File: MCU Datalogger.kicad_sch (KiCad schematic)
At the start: 0 parts

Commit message: Setup of EESchema for new project
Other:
- title: (none) -> ${project_name}
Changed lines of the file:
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@@
 	(generator_version "9.0")
 	(paper "A4")
+	(title_block
+		(title "${project_name}")
+		(date "2025-10-13")
+		(rev "1.0")
+	)
 	(sheet_instances
 		(path "/"

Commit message: Required Symbols Added
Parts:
- added BT1: Battery, symbol Device:Battery
- added C1, C2, C3, C4: C, symbol Device:C
- added C5: C_Polarized, symbol Device:C_Polarized
- added D1, D2: LED, symbol Device:LED
- added H1, H2, H3, H4: MountingHole, symbol Mechanical:MountingHole
- added R1, R2, R3, R4, R5, R6, R7: R, symbol Device:R
- added U1, U2: 24LC1025, symbol Memory_EEPROM:24LC1025
- added U3: DS1337S_, DS1337S_:SOIC127P600X175-8N, symbol DS1337S_:DS1337S_
- added U4: ATMEGA328P-AU, ATMEGA328P-AU:QFP80P900X900X120-32N, symbol ATMEGA328P-AU:ATMEGA328P-AU
- added Y1, Y2: Crystal, symbol Device:Crystal
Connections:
- new net: U4.21 (GND), U4.3 (GND), U4.5 (GND)
- new net: U4.4 (VCC), U4.6 (VCC)
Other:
- added sheet Connectors (connectors.kicad_sch)

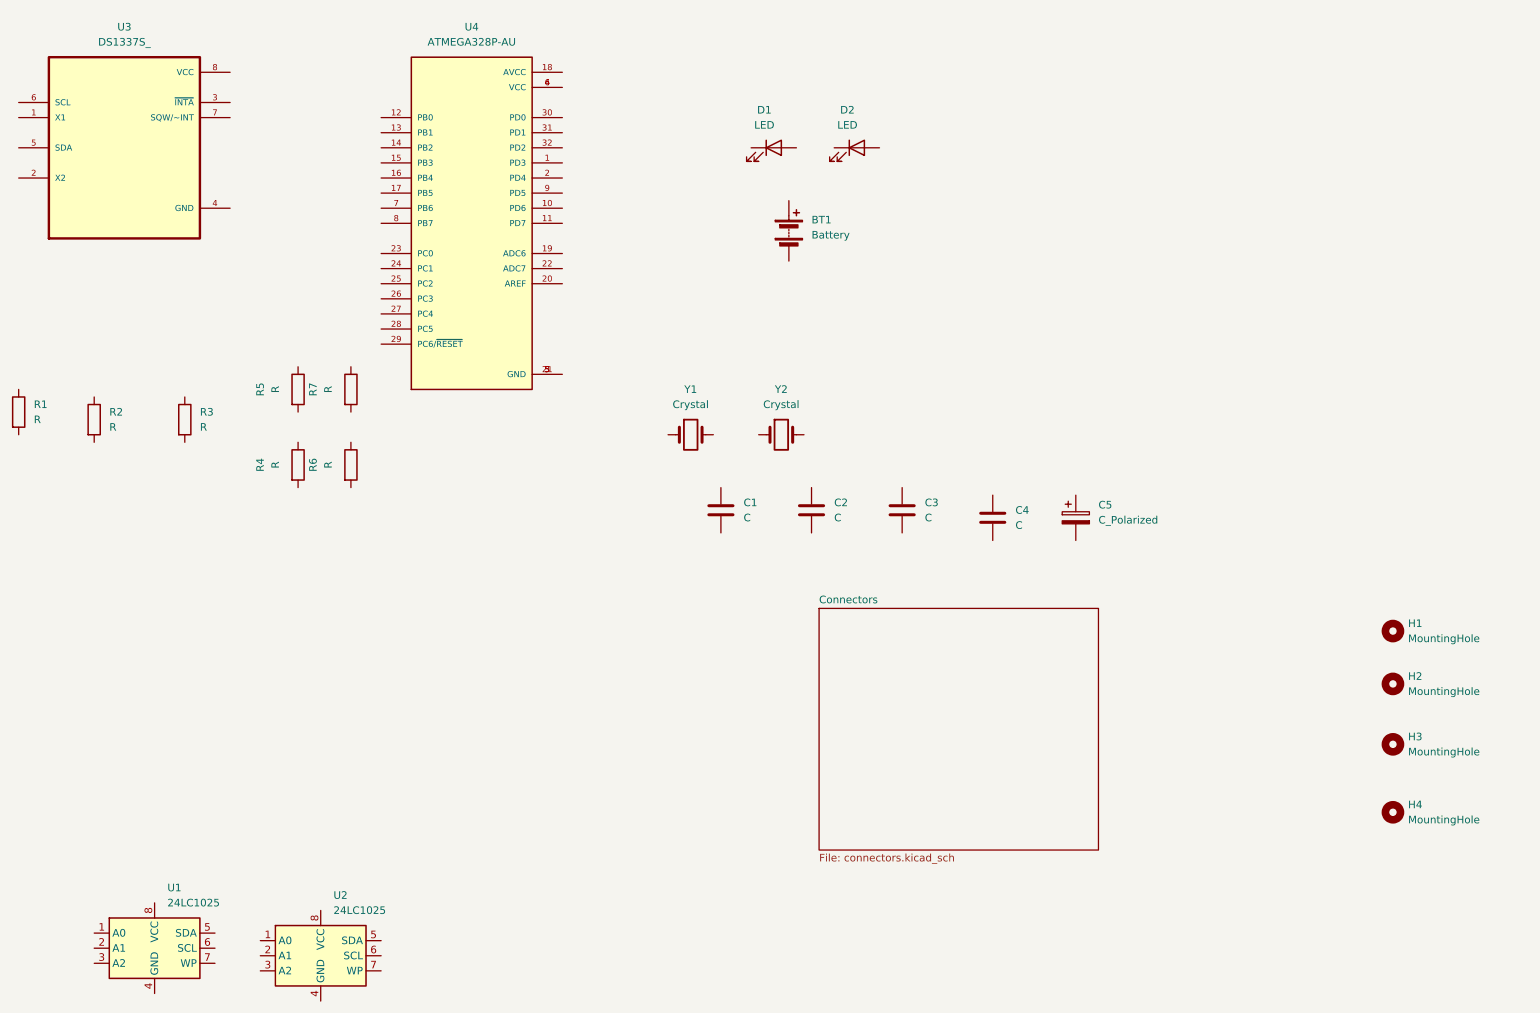
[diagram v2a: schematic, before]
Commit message: Change location of symbols
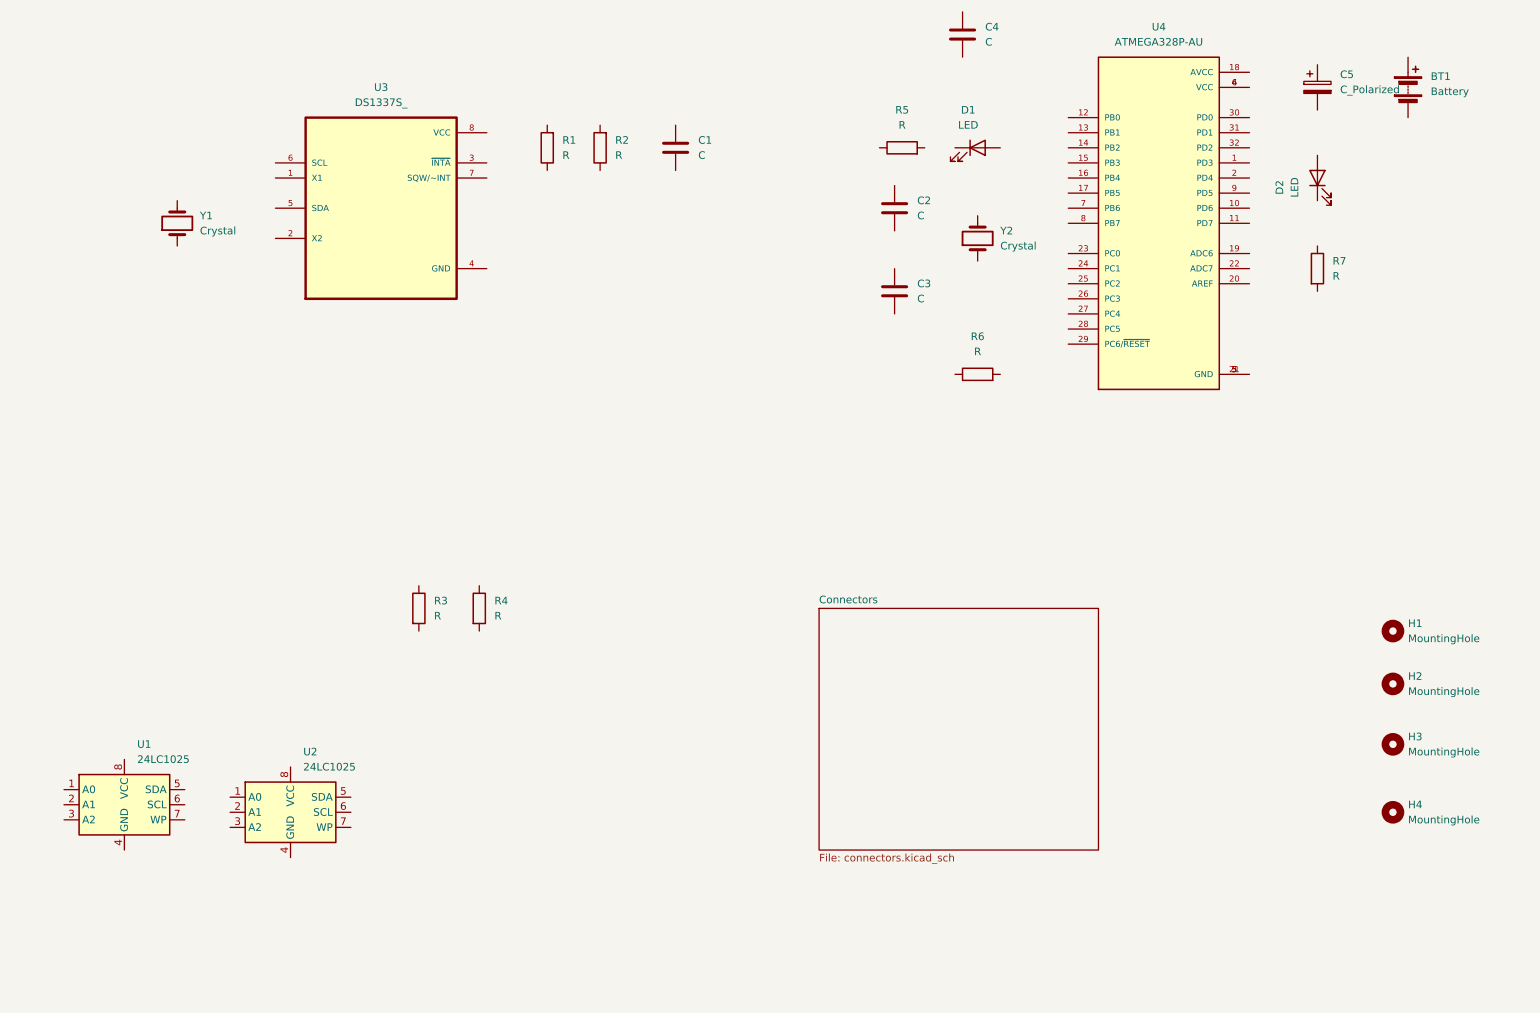
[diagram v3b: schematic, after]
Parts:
- renumbered D2 to D1, D1 to D2, R4 to R1, R6 to R2, R2 to R3, R3 to R4, R7 to R6, R1 to R7
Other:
- moved on the sheet: BT1, C1, C2, C3, C4, C5, D1, D2, R1, R2, R3, R4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

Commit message: Added components values
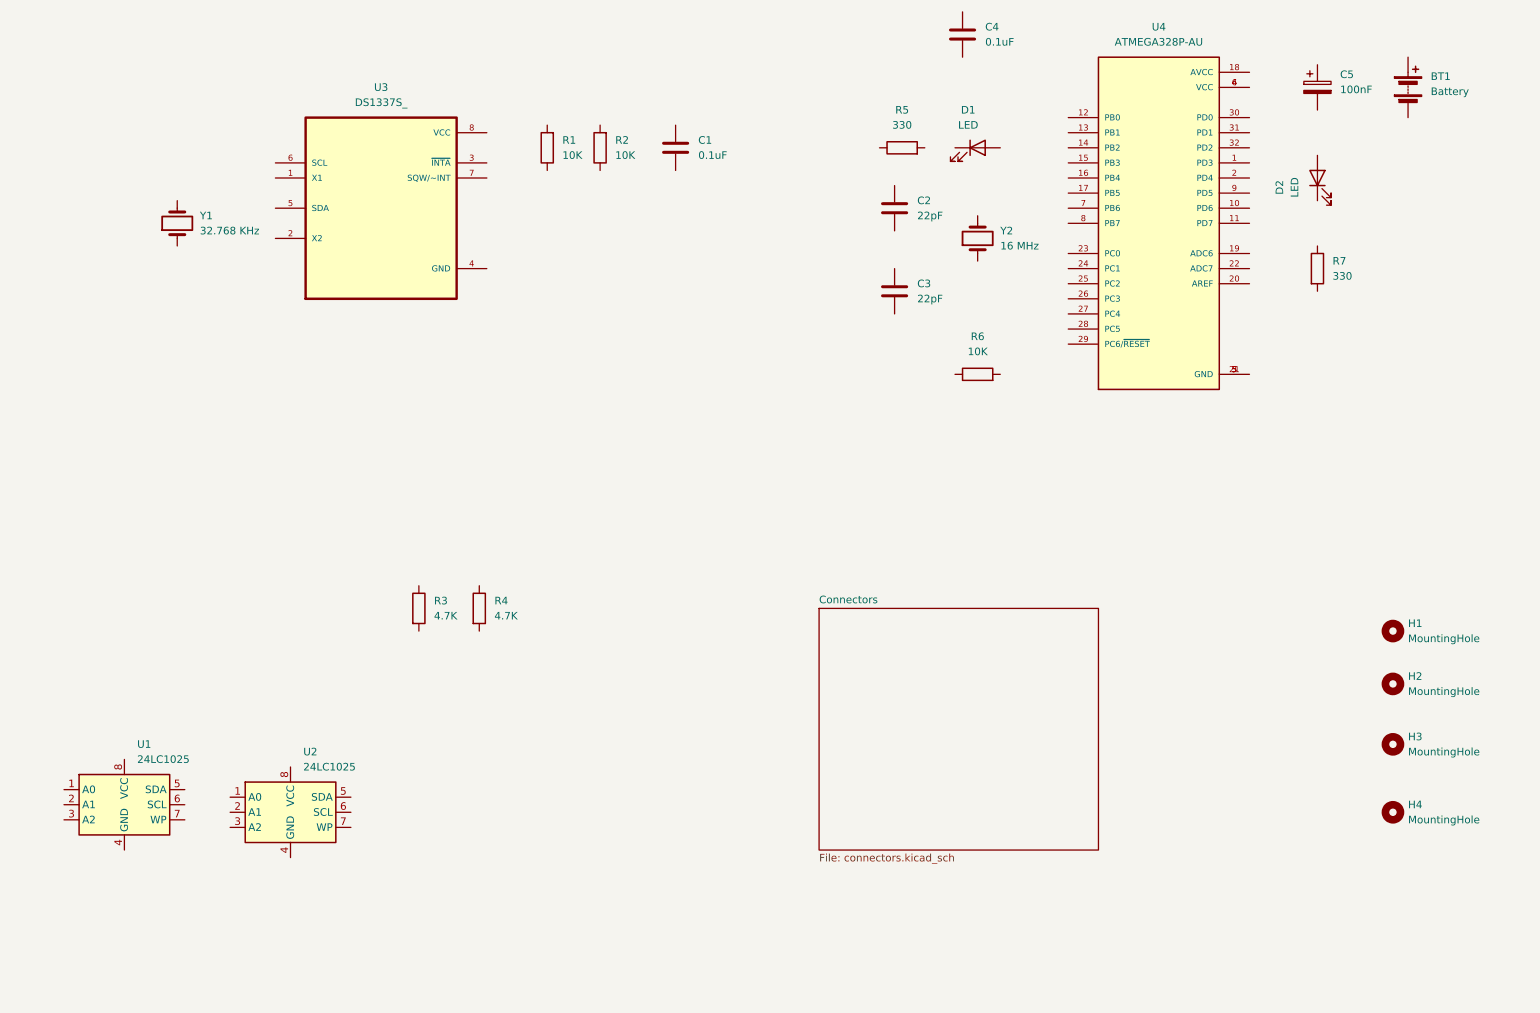
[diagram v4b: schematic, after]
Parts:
- C1, C4: value C -> 0.1uF
- C2, C3: value C -> 22pF
- C5: value C_Polarized -> 100nF
- R1, R2, R6: value R -> 10K
- R3, R4: value R -> 4.7K
- R5, R7: value R -> 330
- Y1: value Crystal -> 32.768 KHz
- Y2: value Crystal -> 16 MHz
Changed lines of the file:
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@@
 			)
 		)
-		(property "Value" "R"
+		(property "Value" "330"
 			(at 168.91 38.1 90)
 			(effects
@@
 			)
 		)
+		(property "Purpose" ""
+			(at 168.91 41.91 0)
+			(effects
+				(font
+					(size 1.27 1.27)
+				)
+				(hide yes)
+			)
+		)
 		(pin "1"
 		)
@@
 			)
 		)
-		(property "Value" "C"
+		(property "Value" "0.1uF"
 			(at 134.62 43.1799 0)
 			(effects
@@
 			)
 		)
+		(property "Purpose" ""
+			(at 130.81 41.91 0)
+			(effects
+				(font
+					(size 1.27 1.27)
+				)
+				(hide yes)
+			)
+		)
 		(pin "1"
 		)
@@
 			)
 		)
-		(property "Value" "R"
+		(property "Value" "10K"
 			(at 111.76 43.1799 0)
 			(effects
@@
 			)
 		)
+		(property "Purpose" ""
+			(at 109.22 41.91 0)
+			(effects
+				(font
+					(size 1.27 1.27)
+				)
+				(hide yes)
+			)
+		)
 		(pin "1"
 		)
@@
 			)
 		)
-		(property "Value" "Crystal"
+		(property "Value" "16 MHz"
 			(at 185.42 58.4199 90)
 			(effects
@@
 			)
 		)
+		(property "Purpose" ""
+			(at 181.61 57.15 0)
+			(effects
+				(font
+					(size 1.27 1.27)
+				)
+				(hide yes)
+			)
+		)
 		(pin "1"
 		)
@@
 			)
 		)
-		(property "Value" "R"
+		(property "Value" "4.7K"
 			(at 100.33 120.6499 0)
 			(effects
@@
 			)
 		)
+		(property "Purpose" ""
+			(at 97.79 119.38 0)
+			(effects
+				(font
+					(size 1.27 1.27)
+				)
+				(hide yes)
+			)
+		)
 		(pin "1"
 		)
@@
 			)
 		)
-		(property "Value" "R"
+		(property "Value" "330"
 			(at 241.3 63.4999 0)
 			(effects
@@
 			)
 		)
+		(property "Purpose" ""
+			(at 238.76 62.23 0)
+			(effects
+				(font
+					(size 1.27 1.27)
+				)
+				(hide yes)
+			)
+		)
 		(pin "1"
 		)
@@
 			)
 		)
-		(property "Value" "Crystal"
+		(property "Value" "32.768 KHz"
 			(at 50.8 55.8799 90)
 			(effects
@@
 			)
 		)
+		(property "Purpose" ""
+			(at 46.99 54.61 0)
+			(effects
+				(font
+					(size 1.27 1.27)
+				)
+				(hide yes)
+			)
+		)
 		(pin "1"
 		)
@@
 			)
 		)
-		(property "Value" "R"
+		(property "Value" "10K"
 			(at 181.61 76.2 90)
 			(effects
@@
 			)
 		)
+		(property "Purpose" ""
+			(at 181.61 80.01 0)
+			(effects
+				(font
+					(size 1.27 1.27)
+				)
+				(hide yes)
+			)
+		)
 		(pin "1"
 		)
@@
 			)
 		)
-		(property "Value" "R"
+		(property "Value" "4.7K"
 			(at 90.17 120.6499 0)
 			(effects
@@
 			)
 		)
+		(property "Purpose" ""
+			(at 87.63 119.38 0)
+			(effects
+				(font
+					(size 1.27 1.27)
+				)
+				(hide yes)
+			)
+		)
 		(pin "1"
 		)
@@
 			)
 		)
-		(property "Value" "C"
+		(property "Value" "0.1uF"
 			(at 182.88 24.1299 0)
 			(effects
@@
 			)
 		)
+		(property "Purpose" ""
+			(at 179.07 22.86 0)
+			(effects
+				(font
+					(size 1.27 1.27)
+				)
+				(hide yes)
+			)
+		)
 		(pin "1"
 		)
@@
 			)
 		)
-		(property "Value" "C"
+		(property "Value" "22pF"
 			(at 171.45 67.3099 0)
 			(effects
@@
 			)
 		)
+		(property "Purpose" ""
+			(at 167.64 66.04 0)
+			(effects
+				(font
+					(size 1.27 1.27)
+				)
+				(hide yes)
+			)
+		)
 		(pin "1"
 		)
@@
 			)
 		)
-		(property "Value" "C"
+		(property "Value" "22pF"
 			(at 171.45 53.3399 0)
 			(effects
@@
 			)
 		)
+		(property "Purpose" ""
+			(at 167.64 52.07 0)
+			(effects
+				(font
+					(size 1.27 1.27)
+				)
+				(hide yes)
+			)
+		)
 		(pin "1"
 		)
@@
 			)
 		)
-		(property "Value" "R"
+		(property "Value" "10K"
 			(at 120.65 43.1799 0)
 			(effects
@@
 			)
 		)
+		(property "Purpose" ""
+			(at 118.11 41.91 0)
+			(effects
+				(font
+					(size 1.27 1.27)
+				)
+				(hide yes)
+			)
+		)
 		(pin "1"
 		)
@@
 			)
 		)
-		(property "Value" "C_Polarized"
+		(property "Value" "100nF"
 			(at 242.57 32.1309 0)
 			(effects
@@
 			(at 238.76 31.75 0)
 			(effects
+				(font
+					(size 1.27 1.27)
+				)
+				(hide yes)
+			)
+		)
+		(property "Purpose" ""
+			(at 238.76 31.75 0)
+			(effects

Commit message: Footprints added
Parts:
- BT1: footprint (none) -> Connector_PinHeader_2.54mm:PinHeader_1x02_P2.54mm_Vertical
- C1, C2, C3, C4, C5: footprint (none) -> Capacitor_SMD:C_0805_2012Metric
- D1, D2: footprint (none) -> LED_SMD:LED_0805_2012Metric
- H1, H2, H3, H4: footprint (none) -> MountingHole:MountingHole_2.1mm
- R1, R2, R3, R4, R5, R6, R7: footprint (none) -> Resistor_SMD:R_0805_2012Metric
- U1, U2: footprint (none) -> Package_SO:SOIC-8_5.3x5.3mm_P1.27mm
- U3: footprint DS1337S_:SOIC127P600X175-8N -> Footprints:SOIC127P600X175-8N
- U4: footprint ATMEGA328P-AU:QFP80P900X900X120-32N -> Footprints:QFP80P900X900X120-32N
- Y1, Y2: footprint (none) -> Crystal:Crystal_SMD_5032-2Pin_5.0x3.2mm_HandSoldering
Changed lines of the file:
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@@
 			)
 		)
-		(property "Footprint" ""
+		(property "Footprint" "Connector_PinHeader_2.54mm:PinHeader_1x02_P2.54mm_Vertical"
 			(at 254 30.226 90)
 			(effects
@@
 			)
 		)
-		(property "Footprint" ""
+		(property "Footprint" "MountingHole:MountingHole_2.1mm"
 			(at 251.46 142.24 0)
 			(effects
@@
 			)
 		)
-		(property "Footprint" ""
+		(property "Footprint" "MountingHole:MountingHole_2.1mm"
 			(at 251.46 153.67 0)
 			(effects
@@
 			)
 		)
-		(property "Footprint" ""
+		(property "Footprint" "MountingHole:MountingHole_2.1mm"
 			(at 251.46 132.08 0)
 			(effects
@@
 			)
 		)
-		(property "Footprint" ""
+		(property "Footprint" "LED_SMD:LED_0805_2012Metric"
 			(at 238.76 46.99 0)
 			(effects
@@
 			)
 		)
-		(property "Footprint" ""
+		(property "Footprint" "Resistor_SMD:R_0805_2012Metric"
 			(at 168.91 43.688 90)
 			(effects
@@
 			)
 		)
-		(property "Footprint" "DS1337S_:SOIC127P600X175-8N"
+		(property "Footprint" "Footprints:SOIC127P600X175-8N"
 			(at 81.28 52.07 0)
 			(effects
@@
 			)
 		)
-		(property "Footprint" ""
+		(property "Footprint" "Capacitor_SMD:C_0805_2012Metric"
 			(at 131.7752 45.72 0)
 			(effects
@@
 			)
 		)
-		(property "Footprint" "ATMEGA328P-AU:QFP80P900X900X120-32N"
+		(property "Footprint" "Footprints:QFP80P900X900X120-32N"
 			(at 212.09 54.61 0)
 			(effects
@@
 			)
 		)
-		(property "Footprint" ""
+		(property "Footprint" "Resistor_SMD:R_0805_2012Metric"
 			(at 110.998 41.91 90)
 			(effects
@@
 			)
 		)
-		(property "Footprint" ""
+		(property "Footprint" "Crystal:Crystal_SMD_5032-2Pin_5.0x3.2mm_HandSoldering"
 			(at 181.61 57.15 0)
 			(effects
@@
 			)
 		)
-		(property "Footprint" ""
+		(property "Footprint" "Resistor_SMD:R_0805_2012Metric"
 			(at 96.012 119.38 90)
 			(effects
@@
 			)
 		)
-		(property "Footprint" ""
+		(property "Footprint" "MountingHole:MountingHole_2.1mm"
 			(at 251.46 123.19 0)
 			(effects
@@
 			)
 		)
-		(property "Footprint" ""
+		(property "Footprint" "Resistor_SMD:R_0805_2012Metric"
 			(at 236.982 62.23 90)
 			(effects
@@
 			)
 		)
-		(property "Footprint" ""
+		(property "Footprint" "Crystal:Crystal_SMD_5032-2Pin_5.0x3.2mm_HandSoldering"
 			(at 46.99 54.61 0)
 			(effects
@@
 			)
 		)
-		(property "Footprint" ""
+		(property "Footprint" "Resistor_SMD:R_0805_2012Metric"
 			(at 181.61 81.788 90)
 			(effects
@@
 			)
 		)
-		(property "Footprint" ""
+		(property "Footprint" "Package_SO:SOIC-8_5.3x5.3mm_P1.27mm"
 			(at 38.1 152.4 0)
 			(effects
@@
 			)
 		)
-		(property "Footprint" ""
+		(property "Footprint" "Package_SO:SOIC-8_5.3x5.3mm_P1.27mm"
 			(at 66.04 153.67 0)
 			(effects
@@
 			)
 		)
-		(property "Footprint" ""
+		(property "Footprint" "Resistor_SMD:R_0805_2012Metric"
 			(at 85.852 119.38 90)
 			(effects
@@
 			)
 		)
-		(property "Footprint" ""
+		(property "Footprint" "Capacitor_SMD:C_0805_2012Metric"
 			(at 180.0352 26.67 0)
 			(effects
@@
 			)
 		)
-		(property "Footprint" ""
+		(property "Footprint" "Capacitor_SMD:C_0805_2012Metric"
 			(at 168.6052 69.85 0)
 			(effects
@@
 			)
 		)
-		(property "Footprint" ""
+		(property "Footprint" "Capacitor_SMD:C_0805_2012Metric"
 			(at 168.6052 55.88 0)
 			(effects
@@
 			)
 		)
-		(property "Footprint" ""
+		(property "Footprint" "LED_SMD:LED_0805_2012Metric"
 			(at 181.61 41.91 0)
 			(effects
@@
 			)
 		)
-		(property "Footprint" ""
+		(property "Footprint" "Resistor_SMD:R_0805_2012Metric"
 			(at 119.888 41.91 90)
 			(effects
@@
 			)
 		)
-		(property "Footprint" ""
+		(property "Footprint" "Capacitor_SMD:C_0805_2012Metric"
 			(at 239.7252 35.56 0)
 			(effects
